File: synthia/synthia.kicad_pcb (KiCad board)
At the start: 2 copper layers, 300 x 271.1 mm, 201 parts, among them J1 MJ-63022B, J2 SJ3-35083C-TR, J3 PJ-007, J4 SDS-50J, Q1 IRF9540N, U1 TLV272IP, U2 STM32H750ZBT6, U3 LD1117V33, U4 PVA1EEH31.2NV2, U5 PVA1EEH31.2NV2

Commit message: continued PCB Work, Power circuit is wired
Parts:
- removed the TP19 at (387.8, 216.3)
- removed the TP20 at (387.8, 220.9)
- removed the TP21 at (392.5, 197.7)
- removed TP22: MicroUSB Pin #4, TestPoint:TestPoint_Plated_Hole_D2.0mm
- removed TP23: MicroUSB Pin #5, TestPoint:TestPoint_Plated_Hole_D2.0mm
- added D37: 1N4742A, Diode_THT:D_DO-41_SOD81_P10.16mm_Horizontal, F.Cu at (380.7, 191.6)
- added D39: 1N4742A, Diode_THT:D_DO-41_SOD81_P10.16mm_Horizontal, F.Cu at (380.7, 195.9)
- added D40: 1N4742A, Diode_THT:D_DO-41_SOD81_P10.16mm_Horizontal, F.Cu at (380.7, 200.1)
- added LOGO: LOGO, LOGO, F.Cu at (373.7, 336.0)
- moved TP2 160.4 mm to (249.7, 133.5), turned to 45 degrees
- moved TP13 153.1 mm to (259.1, 126.6)
- moved TP14 150.2 mm to (267.8, 124.7)
- moved TP3 136.3 mm to (271.5, 150.6), turned to 45 degrees
- moved U3 135.9 mm to (261.4, 141.3)
- moved D1 130.3 mm to (255.9, 147.1), turned to 180 degrees
- moved C2 118.2 mm to (271.1, 145.6), turned to 45 degrees
- moved C1 113.4 mm to (264.2, 134.3)
- moved Q1 110.3 mm to (247.2, 142.2)
- moved R2 108.3 mm to (245.2, 150.8)
- moved R15 26.0 mm to (254.1, 166.5)
- moved R16 26.0 mm to (254.1, 180.2)
- moved R17 26.0 mm to (265.5, 166.5)
- moved R18 26.0 mm to (265.5, 164.4)
- moved R19 26.0 mm to (265.5, 180.2)
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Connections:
- J1 pad 4: Net-(U1-1IN+) -> Net-(J1-Pad4)
- J2 pad 2: /DAC_schematic/OUT -> Net-(J1-Pad4)
- J2 pad 5: /DAC_schematic/OUT -> Net-(J1-Pad4)
- J3 pad 1: Net-(J3-Pad1) -> Net-(D40-K)
- TP13 pad 1: Net-(J3-Pad1) -> Net-(D40-K)
- TP4 pad 1: Net-(J3-Pad1) -> Net-(D37-K)
- TP5 pad 1: Net-(J3-Pad1) -> Net-(D39-K)
- TP6 pad 1: Net-(J3-Pad1) -> Net-(D37-A)
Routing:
- net +3.3V: track 0.00 -> 227.7 mm, vias 0 -> 6
- net Net-(Q1-D): track 0.00 -> 123.9 mm, vias 0 -> 2
- net /DAC_schematic/OUT: track 125.7 -> 46.8 mm
- net Net-(J3-Pad3): track 0.00 -> 51.7 mm, vias 0 -> 2
- net Net-(U1-1IN+): track 84.1 -> 33.0 mm, vias 2 -> 0
- net Net-(D40-K): track 0.00 -> 49.9 mm, vias 0 -> 4
- net Net-(J1-Pad4): track 0.00 -> 44.5 mm
- net Net-(D1-K): track 0.00 -> 32.9 mm
- net /DAC_schematic/DAC6: track 81.0 -> 56.9 mm
- net /DAC_schematic/DAC7: track 81.2 -> 57.2 mm
- net /DAC_schematic/DAC3: track 80.6 -> 56.7 mm
- net /DAC_schematic/DAC4: track 80.5 -> 56.7 mm
- net /DAC_schematic/DAC5: track 80.5 -> 56.7 mm
- net /DAC_schematic/DAC1: track 80.6 -> 56.9 mm
- net /DAC_schematic/DAC2: track 80.4 -> 56.8 mm
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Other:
- board text added: "+3.3V"
- board text added: "+9V"
- board text added: "AUDIO SCALING"
- board text added: "BAT NEG"
- board text added: "POWER CONVERSION"
- board text added: "REV 1.0"

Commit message: More PCB Work, Button Matrix fully routed and strumpad wiring done
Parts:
- D37, D39, D40: value 1N4742A -> 1N4001
- moved D37 229.6 mm to (151.2, 198.9)
- moved D39 229.6 mm to (151.2, 203.1)
- moved D40 229.6 mm to (151.2, 207.4)
- moved R51 229.1 mm to (123.0, 183.0)
- moved R52 229.1 mm to (123.0, 187.2)
- moved R53 229.1 mm to (123.0, 191.5)
- moved R54 229.1 mm to (123.0, 195.8)
- moved R55 229.1 mm to (123.0, 200.1)
- moved R56 229.1 mm to (123.0, 204.3)
- moved R57 229.1 mm to (123.0, 208.6)
- moved R58 229.1 mm to (123.0, 212.9)
- moved R59 229.1 mm to (123.0, 217.2)
- moved R60 229.1 mm to (123.0, 221.5)
- moved R61 229.1 mm to (123.0, 225.7)
- moved R62 229.1 mm to (123.0, 230.0)
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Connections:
- D39 pad 1: Net-(D39-K) -> Net-(D37-K)
- D39 pad 2: Net-(D37-K) -> Net-(D39-A)
- D40 pad 1: Net-(D40-K) -> Net-(D37-K)
- D40 pad 2: Net-(D39-K) -> Net-(D40-A)
- J3 pad 1: Net-(D40-K) -> Net-(D37-K)
- TP13 pad 1: Net-(D40-K) -> Net-(D37-K)
- TP4 pad 1: Net-(D37-K) -> Net-(D39-A)
- TP5 pad 1: Net-(D39-K) -> Net-(D40-A)
- U2 pad 111: unconnected-(U2B-PC10-Pad111) -> /Button_Matrix/ScanRow2
- U2 pad 112: unconnected-(U2B-PC11-Pad112) -> /Button_Matrix/ScanRow1
- U2 pad 113: unconnected-(U2B-PC12-Pad113) -> /Button_Matrix/ScanRow0
- U2 pad 73: unconnected-(U2B-PB12-Pad73) -> /Button_Matrix/ScanCol0
- U2 pad 74: unconnected-(U2B-PB13-Pad74) -> /Button_Matrix/ScanCol1
- U2 pad 75: unconnected-(U2B-PB14-Pad75) -> /Button_Matrix/ScanCol2
- U2 pad 76: unconnected-(U2B-PB15-Pad76) -> /Button_Matrix/ScanCol3
- U2 pad 77: unconnected-(U2B-PD8-Pad77) -> /Button_Matrix/ScanCol4
- U2 pad 78: unconnected-(U2B-PD9-Pad78) -> /Button_Matrix/ScanCol5
- U2 pad 79: unconnected-(U2B-PD10-Pad79) -> /Button_Matrix/ScanCol6
- U2 pad 80: unconnected-(U2B-PD11-Pad80) -> /Button_Matrix/ScanCol7
- U2 pad 81: unconnected-(U2B-PD12-Pad81) -> /Button_Matrix/ScanCol8
- U2 pad 82: unconnected-(U2B-PD13-Pad82) -> /Button_Matrix/ScanCol9
- U2 pad 85: unconnected-(U2B-PD14-Pad85) -> /Button_Matrix/ScanCol10
- U2 pad 86: unconnected-(U2B-PD15-Pad86) -> /Button_Matrix/ScanCol11
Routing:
- net /Button_Matrix/ScanCol0: track 92.4 -> 272.5 mm, vias 0 -> 2
- net /Button_Matrix/ScanCol1: track 92.6 -> 259.8 mm, vias 0 -> 2
- net /Button_Matrix/ScanCol2: track 92.4 -> 245.4 mm, vias 0 -> 2
- net /Button_Matrix/ScanCol3: track 92.5 -> 231.9 mm, vias 0 -> 2
- net /Button_Matrix/ScanCol4: track 92.3 -> 217.4 mm, vias 0 -> 2
- net /Button_Matrix/ScanCol5: track 92.5 -> 203.8 mm, vias 0 -> 2
- net +3.3V: track 227.7 -> 337.3 mm
- net Net-(U2B-PE1): track 0.00 -> 101.0 mm, vias 0 -> 2
- net /Button_Matrix/ScanCol6: track 92.3 -> 190.0 mm, vias 0 -> 2
- net /Button_Matrix/ScanCol7: track 92.4 -> 175.9 mm, vias 0 -> 2
- net /Button_Matrix/ScanCol8: track 92.4 -> 162.5 mm, vias 0 -> 2
- net /Button_Matrix/ScanRow0: track 251.0 -> 310.7 mm, vias 22 -> 24
- net /Button_Matrix/ScanRow1: track 253.3 -> 311.0 mm, vias 22 -> 24
- net /Button_Matrix/ScanCol9: track 92.4 -> 149.0 mm, vias 0 -> 2
- net Net-(D40-K): track 49.9 -> 0.00 mm, vias 4 -> 0
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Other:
- board text added: "RESET"
- board text added: "USB DEBUG"

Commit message: Again did more Work on the PCB, Battery terminal is wired
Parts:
- moved TP7 241.9 mm to (389.1, 208.9)
- moved TP8 241.4 mm to (389.1, 218.9)
- moved TP9 236.4 mm to (389.1, 228.9)
- moved TP6 234.0 mm to (381.6, 208.9)
- moved TP5 233.2 mm to (381.6, 228.9)
- moved TP4 233.2 mm to (381.6, 218.9)
- moved D40 218.0 mm to (368.1, 228.9)
- moved D39 217.5 mm to (368.1, 218.9)
- moved D37 217.2 mm to (368.1, 208.9)
- moved R39 19.2 mm to (360.4, 177.9), turned to 90 degrees
- moved R50 13.4 mm to (373.4, 127.2), turned to 0 degrees
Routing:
- net Net-(J3-Pad3): track 51.7 -> 233.9 mm, vias 2 -> 4
- net Net-(D37-K): track 49.9 -> 187.9 mm, vias 4 -> 6
- net /Button_Matrix/ScanRow2: track 300.1 -> 295.8 mm
- net Net-(D40-A): track 0.00 -> 3.37 mm
- net Net-(D39-A): track 0.00 -> 3.37 mm
- net Net-(D37-A): track 0.00 -> 3.37 mm
- net GND: vias 0 -> 24
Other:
- board text added: "BAT 1 PWR / GND"
- board text added: "BAT 2 PWR / GND"
- board text added: "BAT 3 PWR / GND"
- board text added: "BATTERY TERMINAL"
- board text added: "STRUMPAD PIN 1 / PWR"
- board text added: "STRUMPAD PIN 2 / OUT"
- board text added: "STRUMPAD PIN 3 / GND"
- board text added: "ScanCol0"
- board text added: "ScanCol1"
- board text added: "ScanCol10"
- board text added: "ScanCol11"
- board text added: "ScanCol2"
- board text added: "ScanCol3"
- board text added: "ScanCol4"
- board text added: "ScanCol5"
- board text added: "ScanCol6"
- board text added: "ScanCol7"
- board text added: "ScanCol8"
- board text added: "ScanCol9"

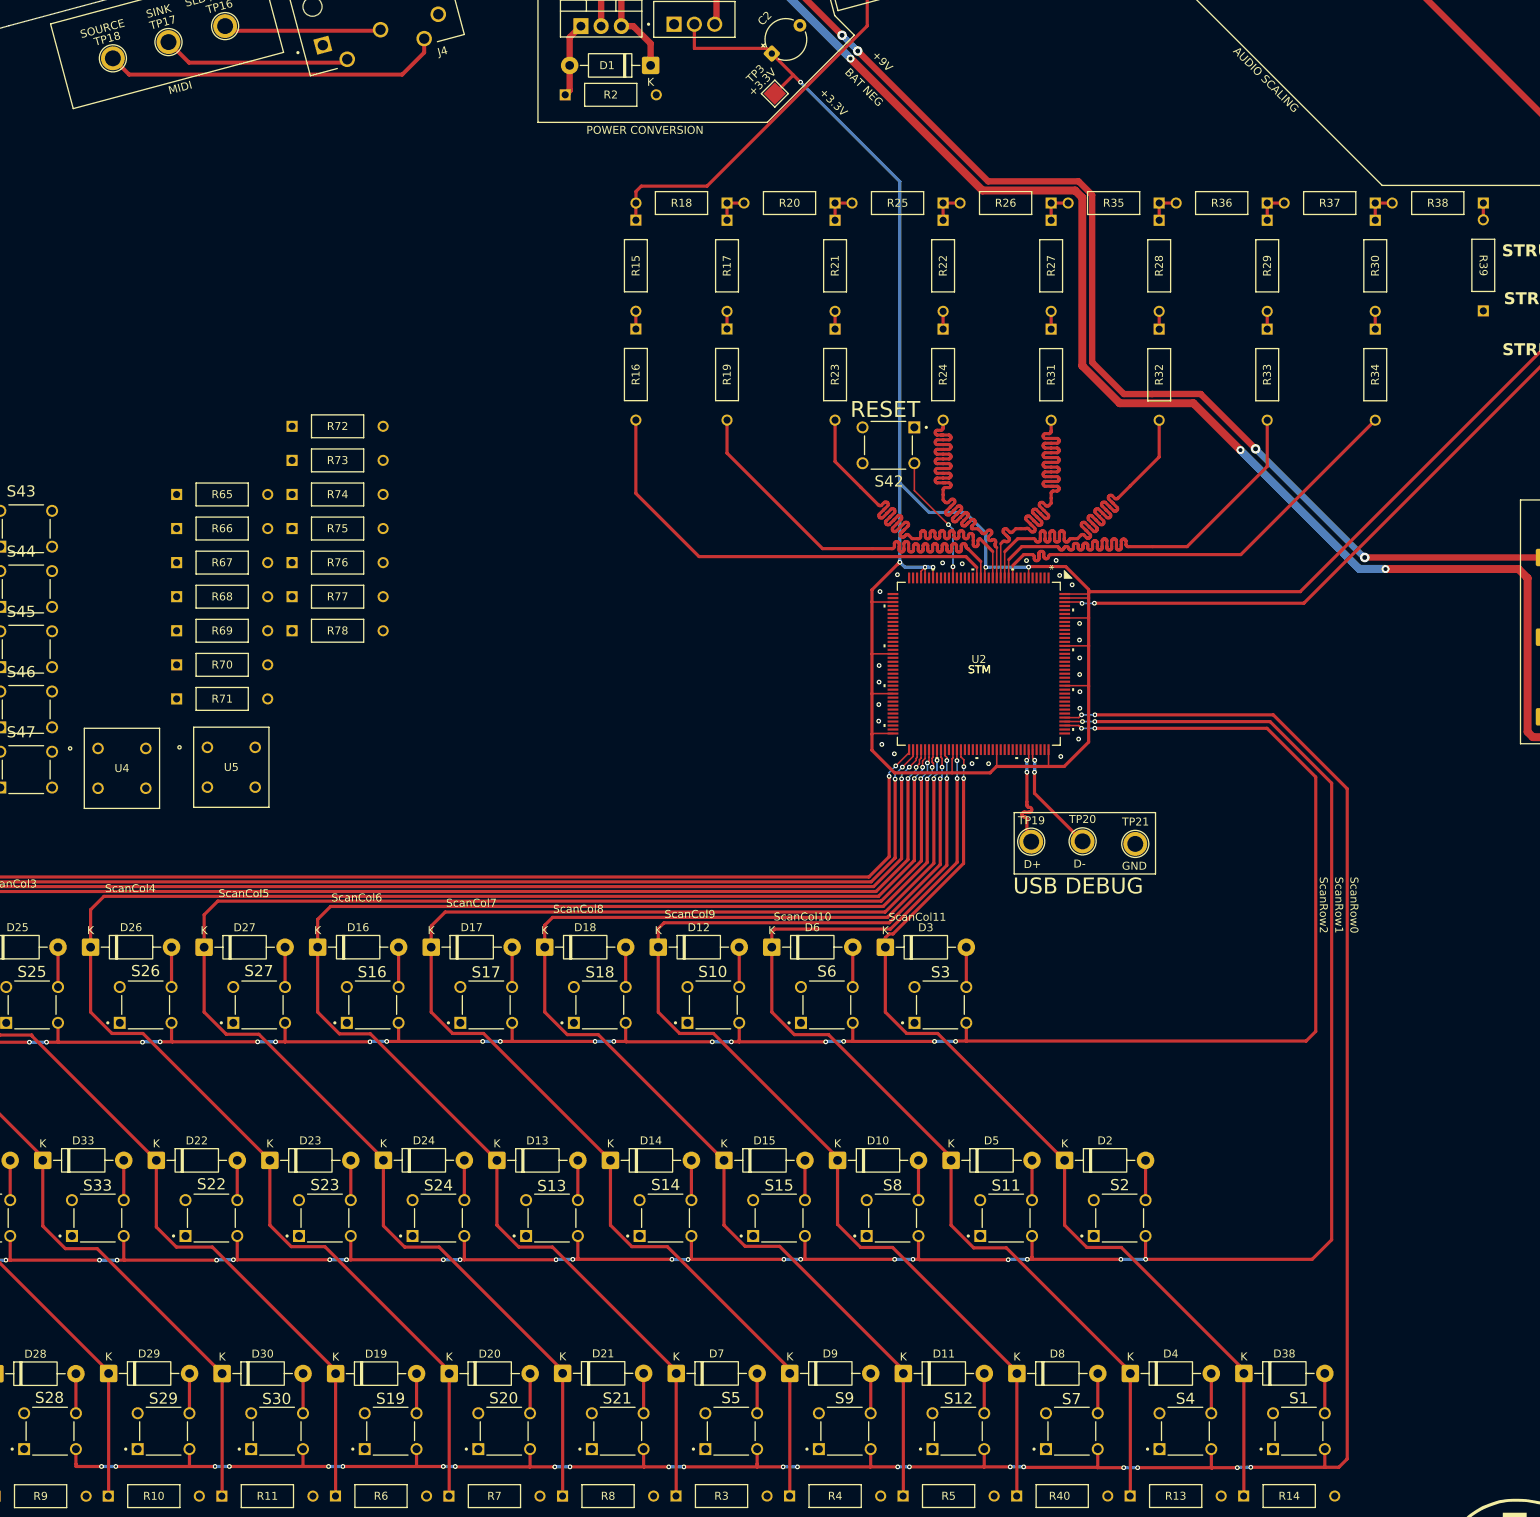
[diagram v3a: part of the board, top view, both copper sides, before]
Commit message: Completely had to redesign most of the pins allocated for power and designed some of the ports that will save us from potentially bricking the stm. PCB wiring for the updated schematic is NOT DONE
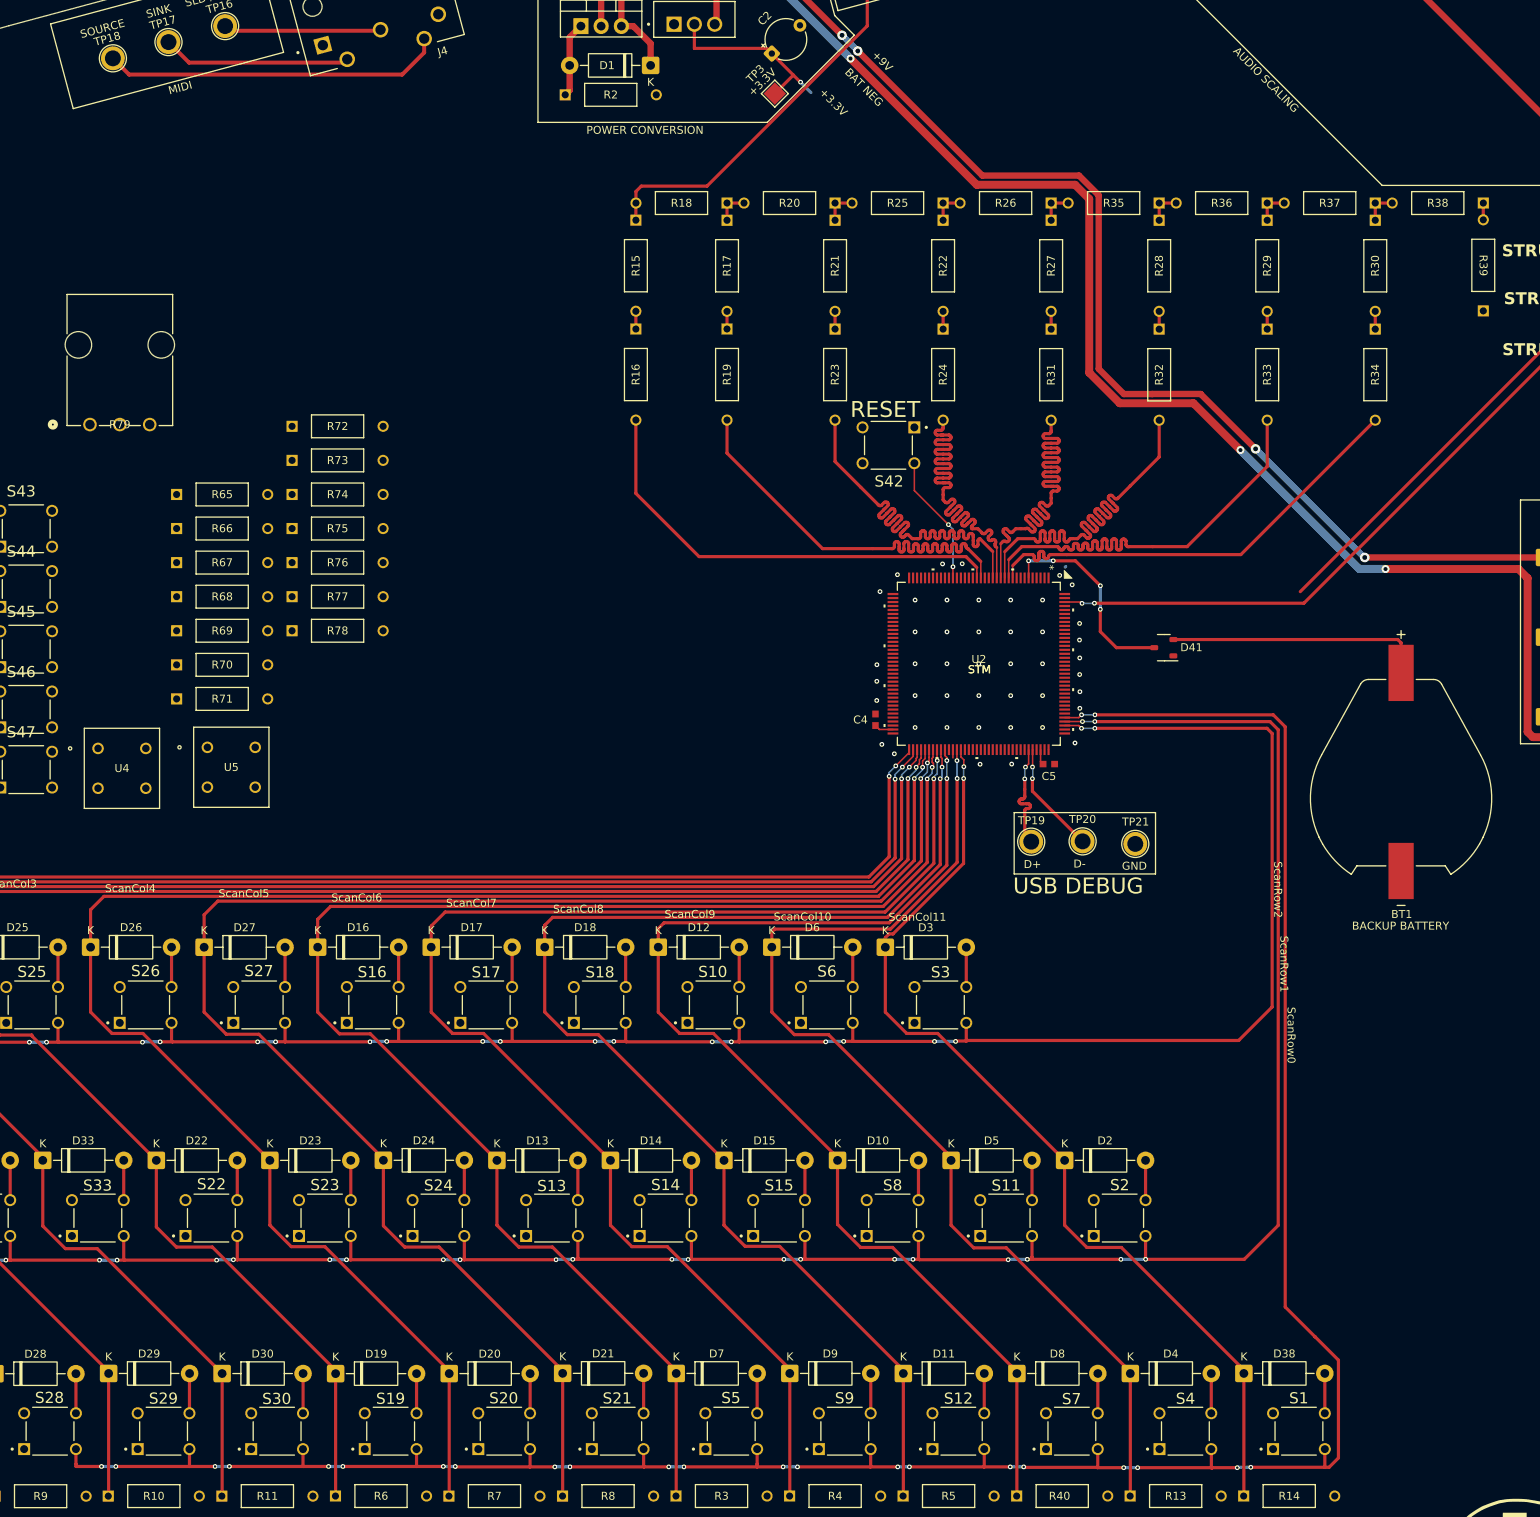
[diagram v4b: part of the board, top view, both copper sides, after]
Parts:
- added BT1: 1063, Synthia_footprint_library:BAT_1063, F.Cu at (350.1, 235.8)
- added C4: GRM188R71A225KE15D, Synthia_footprint_library:G-188_MUR, F.Cu at (284.1, 229.2)
- added C5: GRM188R71A225KE15D, Synthia_footprint_library:G-188_MUR, F.Cu at (305.9, 234.8)
- added D41: BAS70-04, Synthia_footprint_library:P200_SOT-23, F.Cu at (321.5, 221.2)
- added R79: P120PK-Y25BR10K, Synthia_footprint_library:POT_P120PK-x25_TTE, F.Cu at (185.6, 192.2)
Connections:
- U2 pad 106: unconnected-(U2B-VCAP-Pad106) -> Net-(U2B-VCAP)
- U2 pad 6: +3.3V -> Net-(U2A-VBAT)
- U2 pad 71: unconnected-(U2A-VCAP-Pad71) -> Net-(U2A-VCAP)
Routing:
- net +3.3V: track 337.3 -> 98.0 mm, vias 6 -> 1
- net Net-(D41-C): track 0.00 -> 32.5 mm
- net Net-(U2A-VBAT): track 0.00 -> 25.8 mm, vias 0 -> 4
- net /Button_Matrix/ScanRow1: track 311.0 -> 300.4 mm
- net /Button_Matrix/ScanRow2: track 295.8 -> 286.3 mm
- net Net-(U2A-VCAP): track 0.00 -> 2.40 mm
- net Net-(U2B-VCAP): track 0.00 -> 1.94 mm
- net /Button_Matrix/ScanRow0: track 310.7 -> 309.0 mm
- net GND: vias 24 -> 45
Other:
- board text added: "BACKUP BATTERY"
